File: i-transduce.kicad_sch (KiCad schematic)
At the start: 5 parts, among them U1502 ACS730xLCTR-20AB

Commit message: add export of symbol libray, edit symbol links
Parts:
- C1502, C1503: symbol pss:C -> meas:C
- TP1502, TP1503: symbol pss:TestPoint -> meas:TestPoint
- U1502: symbol pss:ACS730xLCTR-20AB -> meas:ACS730xLCTR-20AB
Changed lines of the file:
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@@
 	)
 	(symbol
-		(lib_id "pss:TestPoint")
+		(lib_id "meas:TestPoint")
 		(at 181.61 110.49 0)
 		(unit 1)
@@
 	)
 	(symbol
-		(lib_id "pss:C")
+		(lib_id "meas:C")
 		(at 167.64 115.57 0)
 		(unit 1)
@@
 	)
 	(symbol
-		(lib_id "pss:C")
+		(lib_id "meas:C")
 		(at 144.78 93.98 180)
 		(unit 1)
@@
 	)
 	(symbol
-		(lib_id "pss:ACS730xLCTR-20AB")
+		(lib_id "meas:ACS730xLCTR-20AB")
 		(at 152.4 107.95 0)
 		(unit 1)
@@
 	)
 	(symbol
-		(lib_id "pss:TestPoint")
+		(lib_id "meas:TestPoint")
 		(at 167.64 107.95 0)
 		(unit 1)

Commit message: add export of footprint library, edit footprint links
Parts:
- C1502, C1503: footprint pss:C_0805_2012Metric_Pad1.18x1.45mm_HandSolder -> meas:C_0805_2012Metric_Pad1.18x1.45mm_HandSolder
- TP1502, TP1503: footprint pss:TP_0805_2012Metric -> meas:TP_0805_2012Metric
- U1502: footprint pss:SOIC-8_3.9x4.9mm_P1.27mm -> meas:SOIC-8_3.9x4.9mm_P1.27mm
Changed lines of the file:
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@@
 			)
 		)
-		(property "Footprint" "pss:TP_0805_2012Metric"
+		(property "Footprint" "meas:TP_0805_2012Metric"
 			(at 186.69 110.49 0)
 			(effects
@@
 			)
 		)
-		(property "Footprint" "pss:C_0805_2012Metric_Pad1.18x1.45mm_HandSolder"
+		(property "Footprint" "meas:C_0805_2012Metric_Pad1.18x1.45mm_HandSolder"
 			(at 168.6052 119.38 0)
 			(effects
@@
 			)
 		)
-		(property "Footprint" "pss:C_0805_2012Metric_Pad1.18x1.45mm_HandSolder"
+		(property "Footprint" "meas:C_0805_2012Metric_Pad1.18x1.45mm_HandSolder"
 			(at 143.8148 90.17 0)
 			(effects
@@
 			)
 		)
-		(property "Footprint" "pss:SOIC-8_3.9x4.9mm_P1.27mm"
+		(property "Footprint" "meas:SOIC-8_3.9x4.9mm_P1.27mm"
 			(at 161.29 110.49 0)
 			(effects
@@
 			)
 		)
-		(property "Footprint" "pss:TP_0805_2012Metric"
+		(property "Footprint" "meas:TP_0805_2012Metric"
 			(at 172.72 107.95 0)
 			(effects

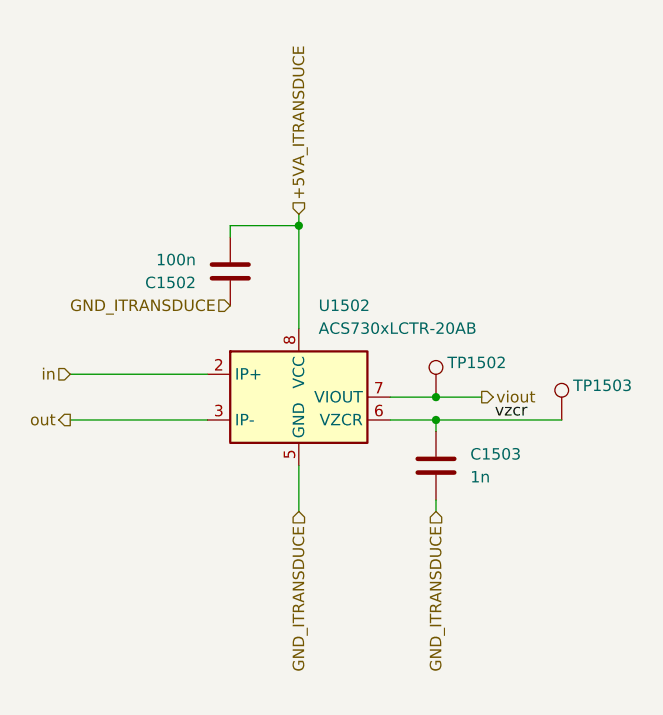
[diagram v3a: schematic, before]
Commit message: add interconnect layout
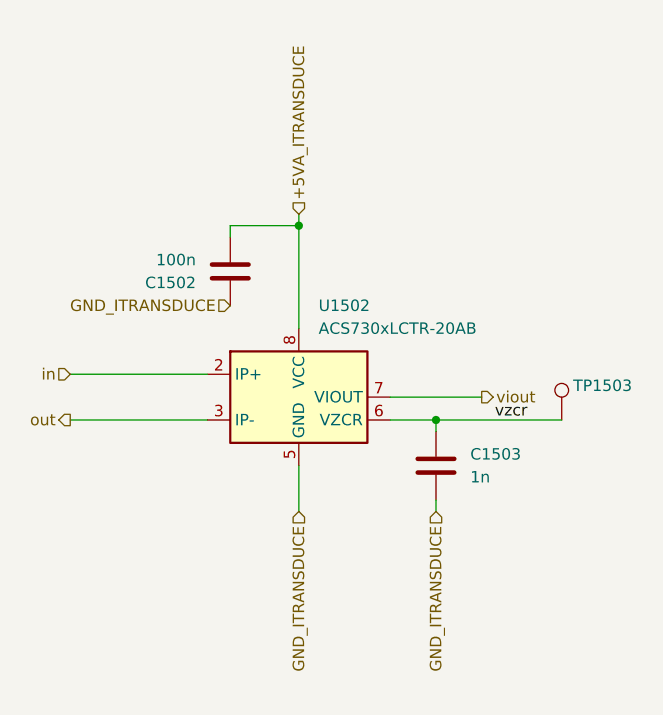
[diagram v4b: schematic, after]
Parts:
- removed TP1502: ~, meas:TP_0805_2012Metric, symbol meas:TestPoint
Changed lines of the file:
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@@
-	)
-	(junction
-		(at 167.64 107.95)
-		(diameter 0)
-		(color 0 0 0 0)
 	)
 	(junction
@@
 	(wire
 		(pts
-			(xy 167.64 107.95) (xy 172.72 107.95)
-		)
-		(stroke
-			(width 0)
-			(type default)
-		)
-	)
-	(wire
-		(pts
-			(xy 162.56 107.95) (xy 167.64 107.95)
+			(xy 162.56 107.95) (xy 172.72 107.95)
 		)
 		(stroke
@@
 					(unit 1)
 				)
-			)
-		)
-	)
-	(symbol
-		(lib_id "meas:TestPoint")
-		(at 167.64 107.95 0)
-		(unit 1)
-		(exclude_from_sim no)
-		(in_bom yes)
-		(on_board yes)
-		(dnp no)
-		(property "Reference" "TP1502"
-			(at 168.91 104.14 0)
-			(effects
-				(font
-					(size 1.27 1.27)
-				)
-				(justify left)
-			)
-		)
-		(property "Value" "~"
-			(at 170.18 105.9179 0)
-			(effects
-				(font
-					(size 1.27 1.27)
-				)
-				(justify left)
-			)
-		)
-		(property "Footprint" "meas:TP_0805_2012Metric"
-			(at 172.72 107.95 0)
-			(effects
-				(font
-					(size 1.27 1.27)
-				)
-				(hide yes)
-			)
-		)
-		(property "Datasheet" "./datasheet/RCTCTE.pdf"
-			(at 172.72 107.95 0)
-			(effects
-				(font
-					(size 1.27 1.27)
-				)
-				(hide yes)
-			)
-		)
-		(property "Description" "test point"
-			(at 167.64 107.95 0)
-			(effects
-				(font
-					(size 1.27 1.27)
-				)
-				(hide yes)
-			)
-		)
-		(property "MPN" "RCTCTE"
-			(at 167.64 107.95 0)
-			(effects
-				(font
-					(size 1.27 1.27)
-				)
-				(hide yes)
-			)
-		)
-		(property "VPN" "660-RCTCTE"
-			(at 167.64 107.95 0)
-			(effects
-				(font
-					(size 1.27 1.27)
-				)
-				(hide yes)
-			)
-		)
-		(pin "1"
-		)
-		(instances
-			(project "pss"
-				(path "/3c438cf7-9350-4e9f-8115-1deba8984176/930a3603-b5c1-4234-96f5-716c518f6fe1"
-					(reference "TP1502")
-					(unit 1)
-				)
-			)
-			(project "meas"
-				(path "/f710e4da-f895-4fe1-9122-3234febe82c7/d8b83012-dd63-42fd-bab5-7d89e6ad661d"
-					(reference "TP901")
-					(unit 1)
-				)
